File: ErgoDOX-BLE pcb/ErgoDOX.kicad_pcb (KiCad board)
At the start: 2 copper layers, 182.8 x 158.9 mm, 110 parts, among them J1 Conn_01x04, J2 Conn_01x02_Female, J3 Conn_01x02_Female, J4 Conn_01x02, J5 Conn_01x02, P1 USB_C_Plug_USB2.0, Q1 Q_NPN_BCE, SW0:10 SW0:3, SW0:11 SW0:2, SW0:12 SW0:1, SW0:7 SW0:6, SW0:8 SW0:5, SW0:9 SW0:4, SW1:10 SW1:3, SW1:11 SW1:2, SW1:12 SW1:1, SW1:13 SW1:0, SW1:9 SW1:4, SW2:10 SW2:3, SW2:11 SW2:2, SW2:12 SW2:1, SW2:13 SW2:0, SW2:7 SW2:6, SW2:8 SW2:5, SW2:9 SW2:4, SW3:10 SW3:3, SW3:11 SW3:2, SW3:12 SW3:1, SW3:13 SW3:0, SW3:8 SW3:5, SW3:9 SW3:4, SW4:10 SW4:3, SW4:11 SW4:2, SW4:12 SW4:1, SW4:13 SW4:0, SW4:7 SW4:6, SW4:8 SW4:5, SW4:9 SW4:4, SW5:10 SW5:3, SW5:11 SW5:2, SW5:12 SW5:1, SW5:13 SW5:0, SW5:7 SW5:6, SW5:8 SW5:5, SW5:9 SW5:4, U1 MCP23018, U3 C0720B001F

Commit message: Rule checking woohoo
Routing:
- net /COL2: track 258.2 -> 284.3 mm, vias 0 -> 2
- net /COL3: track 212.0 -> 236.0 mm, vias 2 -> 3
- net Net-(SW2:9-Pad2): track 0.00 -> 22.9 mm
- net /ROW2: track 271.7 -> 253.9 mm
- net /COL5: track 222.0 -> 235.6 mm
- net /ROW3: track 198.1 -> 208.9 mm
- net /COL4: track 287.3 -> 292.5 mm
- net /COL1: track 349.8 -> 352.3 mm
- net Net-(SW4:13-Pad2): track 23.6 -> 21.3 mm
- net Net-(SW3:11-Pad2): track 14.7 -> 16.5 mm
- net /EncoderPin2: track 181.2 -> 182.8 mm
- net /ROW5: track 269.6 -> 270.7 mm
- net Net-(SW0:10-Pad2): track 25.4 -> 24.5 mm

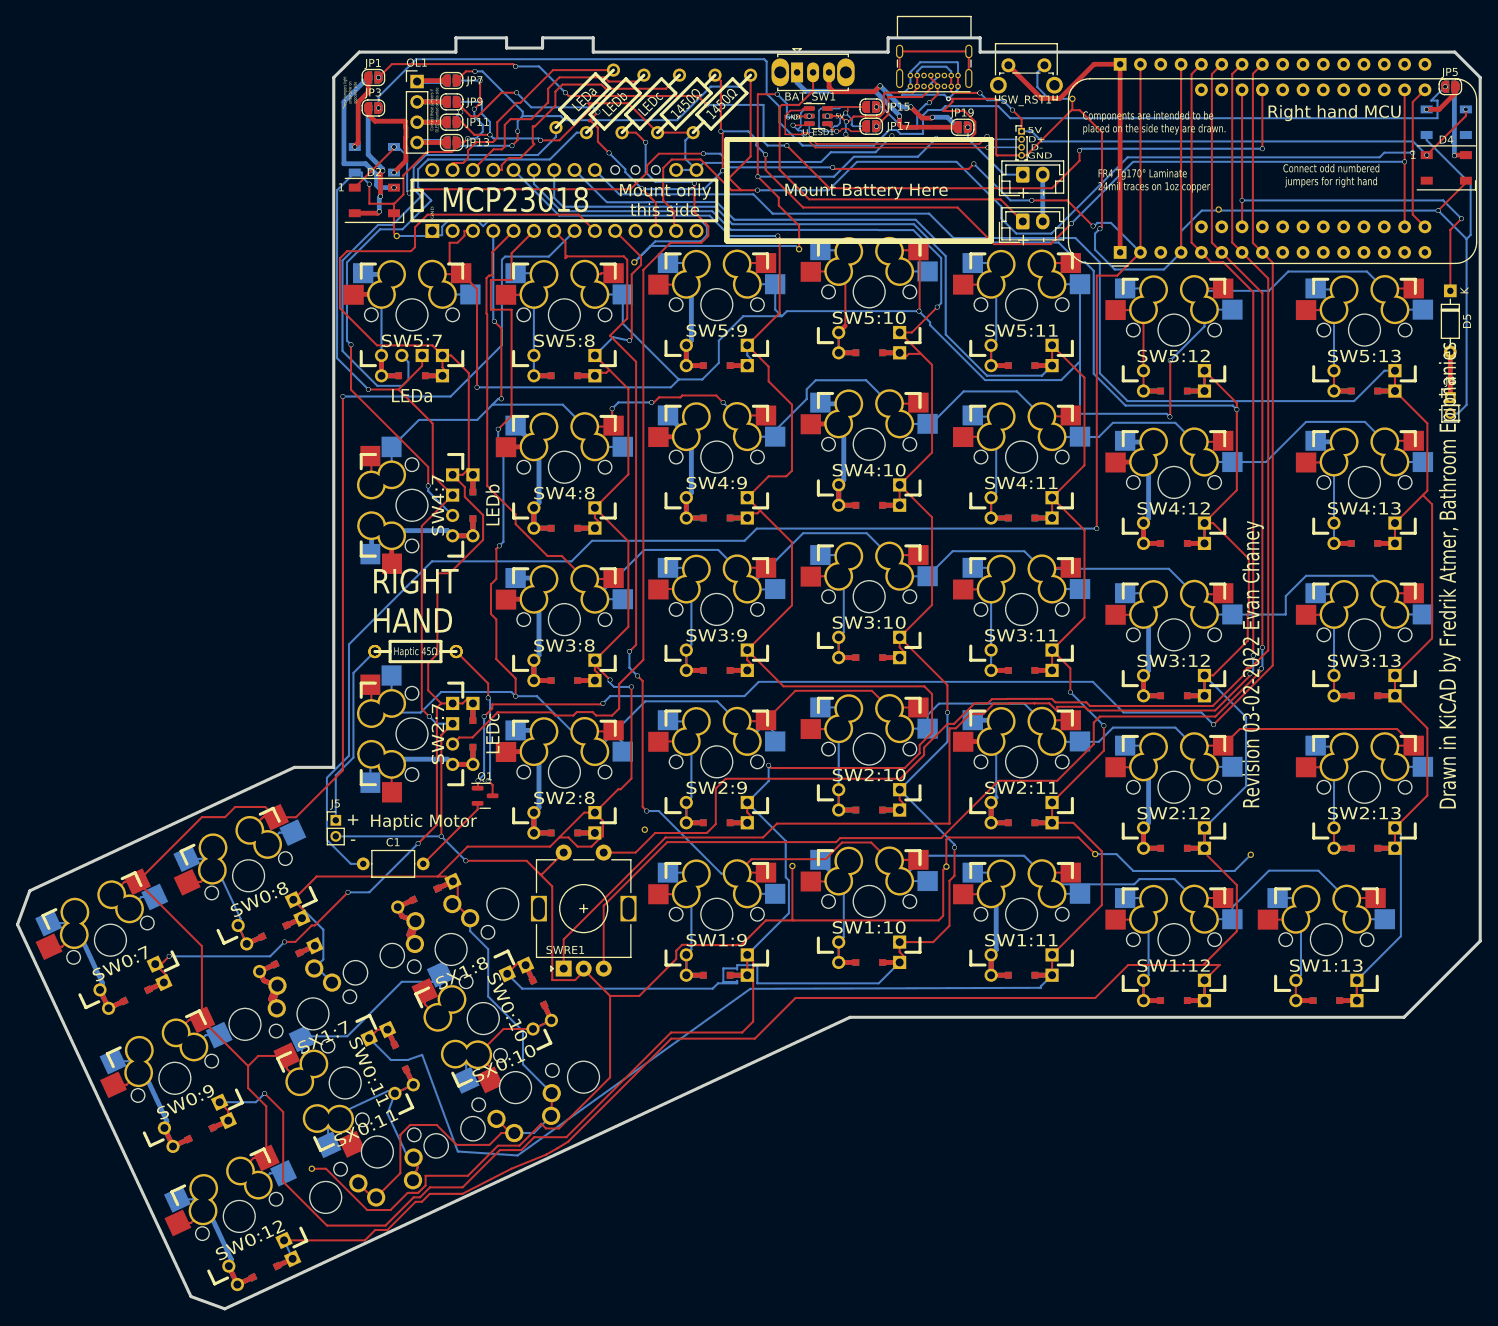
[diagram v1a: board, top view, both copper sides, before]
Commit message: Add some holes and route around them!
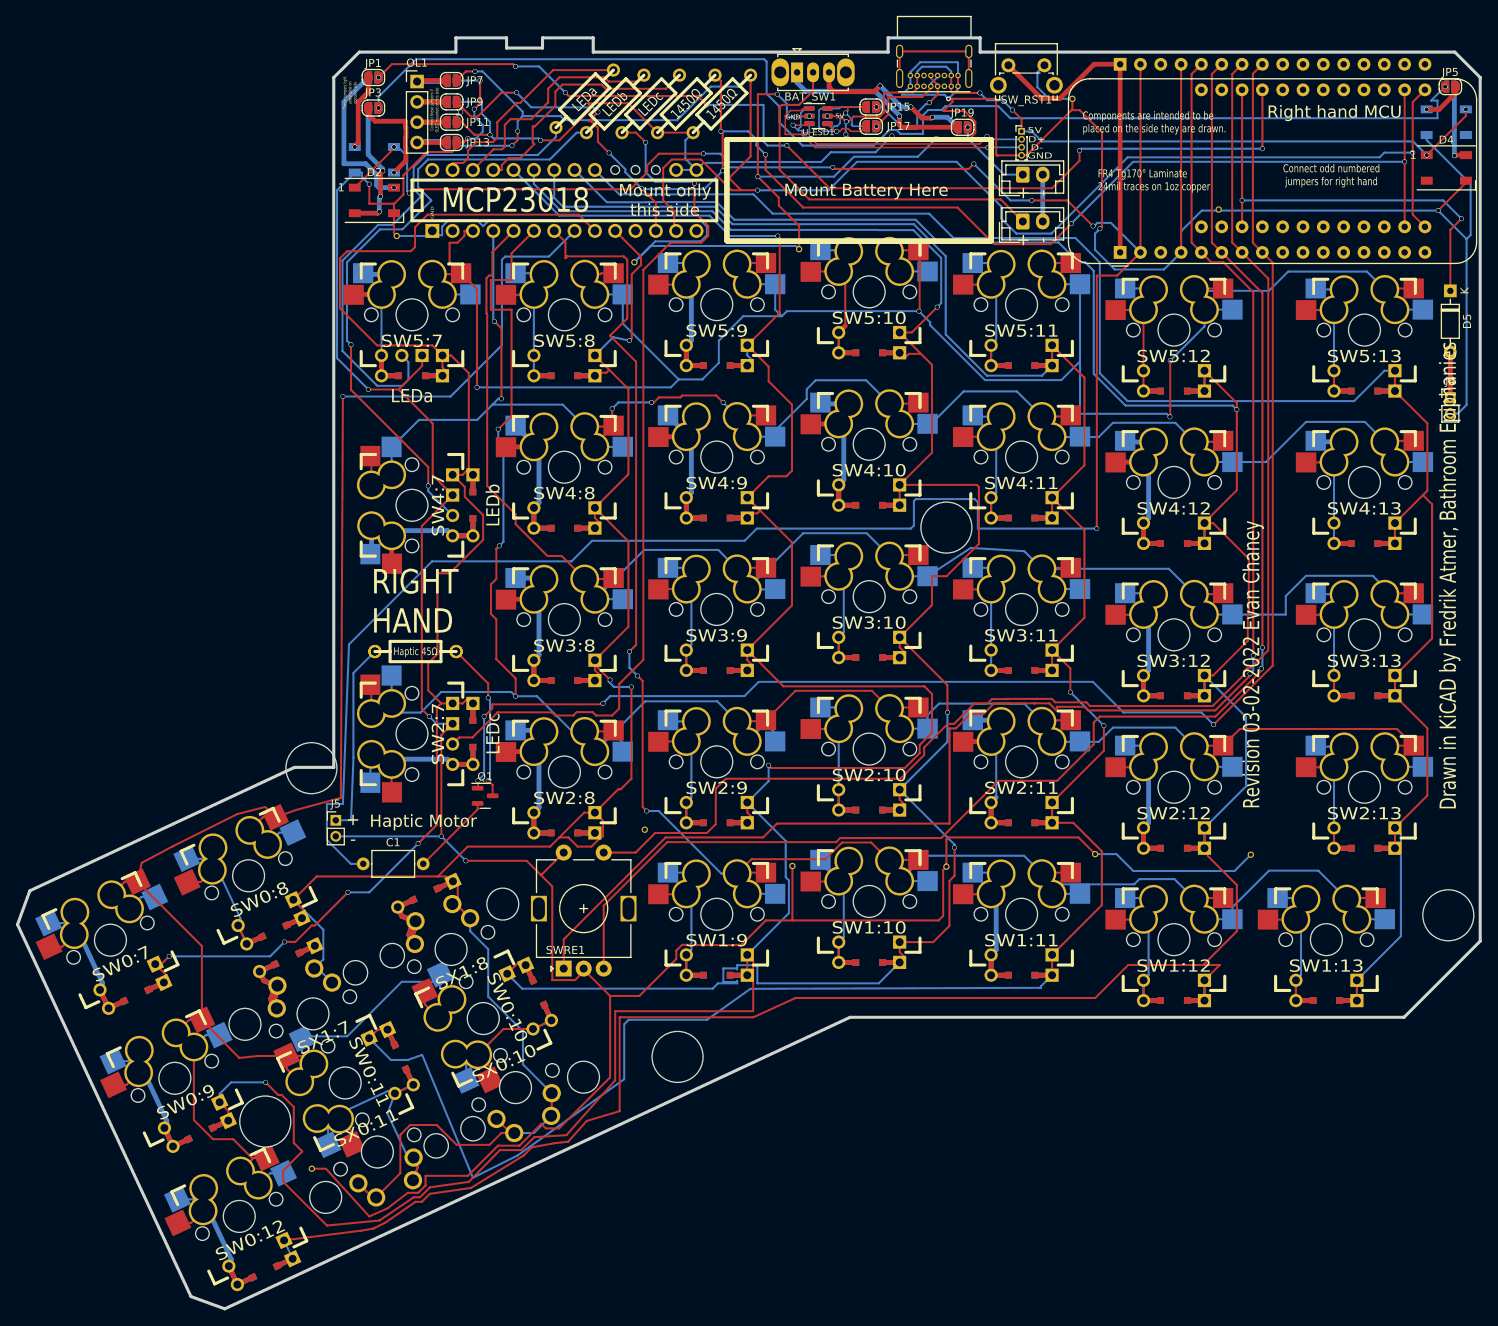
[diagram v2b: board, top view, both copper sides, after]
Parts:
- added ?: , , F.Cu at (59.8, 121.8)
- added ?: , , F.Cu at (201.9, 140.2)
- added ?: , , F.Cu at (139.2, 91.7)
- added ?: , , F.Cu at (105.6, 157.9)
- added ?: , , F.Cu at (54.1, 165.9)
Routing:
- net /COL3: track 236.0 -> 247.5 mm
- net /ROW0: track 241.2 -> 252.5 mm
- net /COL4: track 292.5 -> 301.1 mm
- net +3V3: track 304.2 -> 311.6 mm
- net /COL2: track 284.3 -> 291.5 mm
- net /COL1: track 352.3 -> 357.7 mm
- net Net-(J5-Pad1): track 23.1 -> 24.1 mm

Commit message: a touch more routing
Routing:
- net /SCL: track 179.6 -> 180.3 mm
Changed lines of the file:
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@@
   (segment (start 110.998 35.868796) (end 110.272102 35.142898) (width 0.254) (layer "F.Cu") (net 89))
   (segment (start 95.469144 39.918577) (end 95.631 39.756721) (width 0.254) (layer "F.Cu") (net 89))
+  (segment (start 79.291059 39.764059) (end 78.008 38.481) (width 0.254) (layer "F.Cu") (net 89))
   (segment (start 80.604789 40.299211) (end 83.566 37.338) (width 0.254) (layer "F.Cu") (net 89))
   (segment (start 94.791361 40.898506) (end 94.489215 40.898506) (width 0.254) (layer "F.Cu") (net 89))
@@
   (segment (start 196.469 54.102) (end 196.469 36.9765) (width 0.254) (layer "F.Cu") (net 89))
   (segment (start 116.586 45.085) (end 116.586 46.99) (width 0.254) (layer "F.Cu") (net 89))
-  (segment (start 78.486 39.751) (end 78.486 38.959) (width 0.254) (layer "F.Cu") (net 89))
   (segment (start 110.998 42.164) (end 110.998 35.868796) (width 0.254) (layer "F.Cu") (net 89))
   (segment (start 102.87 51.079444) (end 101.079278 49.288722) (width 0.254) (layer "F.Cu") (net 89))
@@
   (segment (start 78.486 39.029882) (end 79.755329 40.299211) (width 0.254) (layer "F.Cu") (net 89))
   (segment (start 97.028 44.86338) (end 95.627709 43.463089) (width 0.254) (layer "F.Cu") (net 89))
-  (segment (start 78.486 38.959) (end 78.008 38.481) (width 0.254) (layer "F.Cu") (net 89))
   (segment (start 121.285 51.689) (end 140.58445 51.689) (width 0.254) (layer "F.Cu") (net 89))
   (segment (start 111.2261 42.3921) (end 111.2261 47.0911) (width 0.254) (layer "F.Cu") (net 89))
+  (segment (start 79.291059 39.834941) (end 79.291059 39.764059) (width 0.254) (layer "F.Cu") (net 89))
   (via (at 101.079278 49.288722) (size 0.6096) (drill 0.508) (layers "F.Cu" "B.Cu") (net 89))
   (via (at 97.028 44.86338) (size 0.6096) (drill 0.508) (layers "F.Cu" "B.Cu") (net 89))
   (via (at 154.797969 53.705969) (size 0.6096) (drill 0.508) (layers "F.Cu" "B.Cu") (net 89))
   (via (at 196.469 45.974) (size 0.6096) (drill 0.508) (layers "F.Cu" "B.Cu") (net 89))
-  (via (at 78.486 39.751) (size 0.6096) (drill 0.508) (layers "F.Cu" "B.Cu") (net 89))
+  (via (at 79.291059 39.834941) (size 0.6096) (drill 0.508) (layers "F.Cu" "B.Cu") (net 89))
   (via (at 110.998 42.164) (size 0.6096) (drill 0.508) (layers "F.Cu" "B.Cu") (net 89))
   (via (at 116.586 45.085) (size 0.6096) (drill 0.508) (layers "F.Cu" "B.Cu") (net 89))
@@
   (segment (start 99.06 46.89538) (end 99.06 47.269443) (width 0.254) (layer "B.Cu") (net 89))
   (segment (start 95.040684 39.160684) (end 87.293684 39.160684) (width 0.254) (layer "B.Cu") (net 89))
-  (segment (start 77.993 41.021) (end 77.993 40.244) (width 0.254) (layer "B.Cu") (net 89))
   (segment (start 87.293684 39.160684) (end 85.471 37.338) (width 0.254) (layer "B.Cu") (net 89))
   (segment (start 108.92952 49.38768) (end 111.2261 47.0911) (width 0.254) (layer "B.Cu") (net 89))
@@
   (segment (start 99.06 47.269443) (end 101.178237 49.38768) (width 0.254) (layer "B.Cu") (net 89))
   (segment (start 114.427 42.164) (end 110.998 42.164) (width 0.254) (layer "B.Cu") (net 89))
+  (segment (start 79.291059 39.834941) (end 79.179059 39.834941) (width 0.254) (layer "B.Cu") (net 89))
   (segment (start 116.586 45.085) (end 115.42768 43.92668) (width 0.254) (layer "B.Cu") (net 89))
   (segment (start 115.42768 43.16468) (end 114.427 42.164) (width 0.254) (layer "B.Cu") (net 89))
   (segment (start 97.028 44.86338) (end 99.06 46.89538) (width 0.254) (layer "B.Cu") (net 89))
-  (segment (start 77.993 40.244) (end 78.486 39.751) (width 0.254) (layer "B.Cu") (net 89))
+  (segment (start 79.179059 39.834941) (end 77.993 41.021) (width 0.254) (layer "B.Cu") (net 89))
   (segment (start 133.35 143.51) (end 133.35 144.764311) (width 0.254) (layer "F.Cu") (net 90))
   (segment (start 133.35 106.664311) (end 133.992845 107.307156) (width 0.254) (layer "F.Cu") (net 90))
